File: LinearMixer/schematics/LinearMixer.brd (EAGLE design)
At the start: 49.7 x 98.7 mm, 65 parts, among them IC1 QUAD_OPAMPD, IC2 QUAD_OPAMPD, X1 53048-05, X2 53048-05, X5 53048-03, X6 53048-03, X7 53048-03

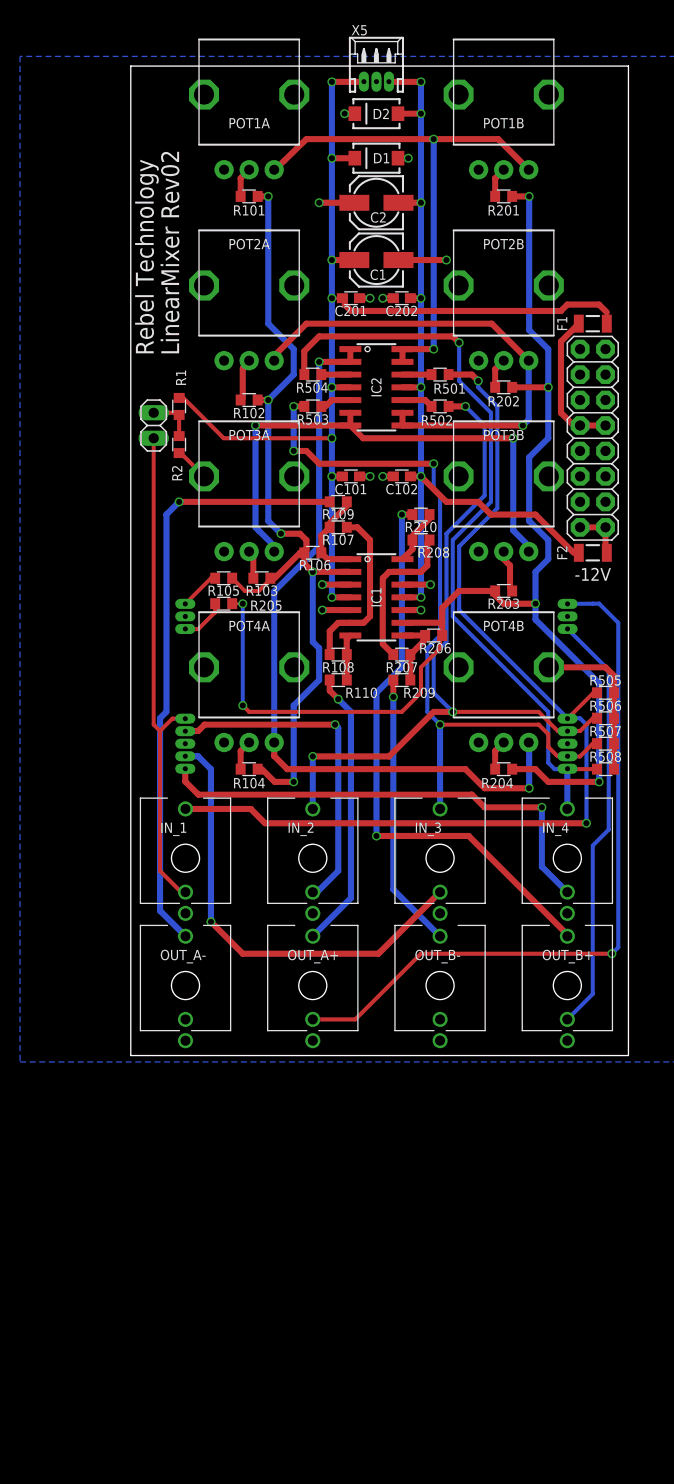
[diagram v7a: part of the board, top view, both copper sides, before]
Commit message: changed inverting outputs to hp
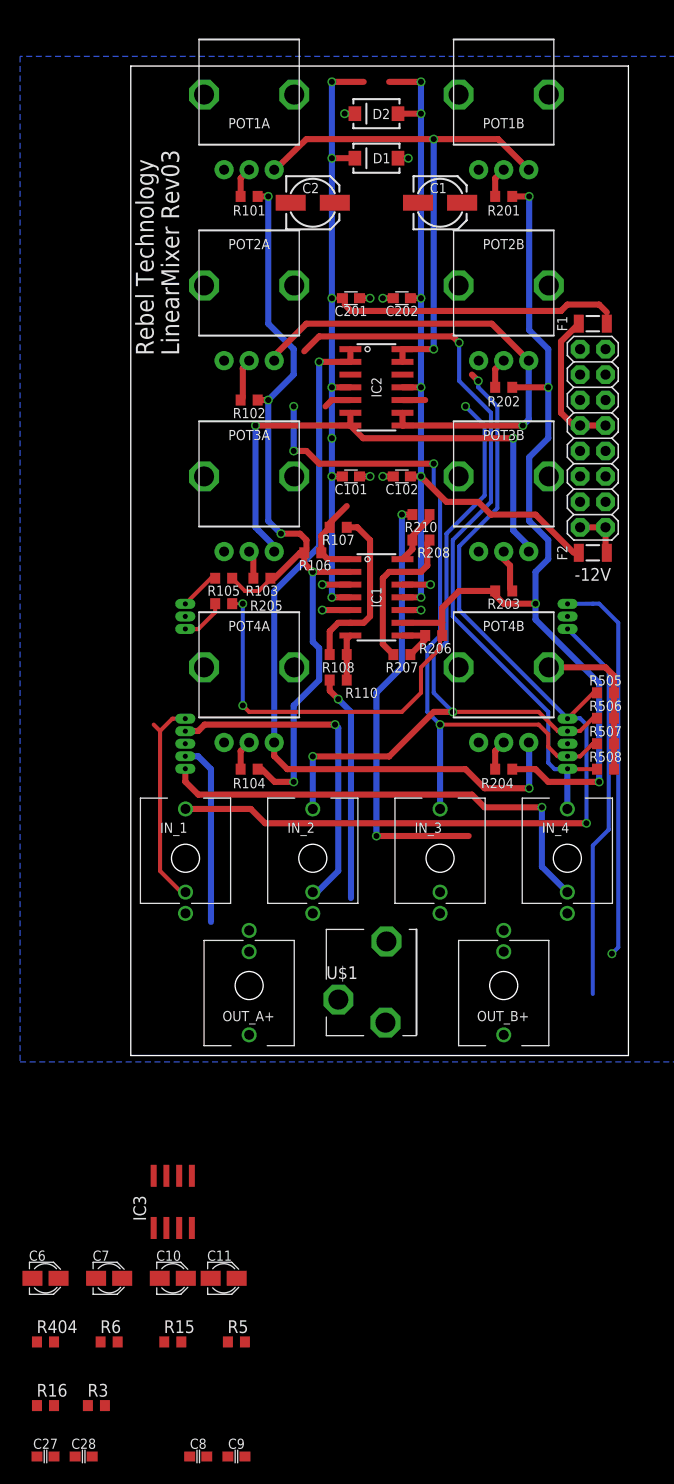
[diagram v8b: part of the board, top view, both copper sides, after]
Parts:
- removed JP1: (no value), pinhead:1X02
- removed OUT_A-, OUT_B-: THONKICONN, Rebel:THONKICONN
- removed R1, R2: 10k, resistor:R0603
- removed R109, R209: 100R, resistor:R0603
- removed R501, R502, R503, R504: 1k, resistor:R0603
- removed X5: 53048-03, con-molex:53048-03
- added C10, C11: 1uF, rcl:PANASONIC_A
- added C27, C28: 0.1uF, Rebel:C0603
- added C6, C7: 220uF, rcl:PANASONIC_A
- added C8, C9: 47nF, Rebel:C0603
- added IC3: NE5532D, linear:SO08
- added R15, R6: 100k, resistor:R0603
- added R16, R5: 4.7k, resistor:R0603
- added R3, R404: 10R, resistor:R0603
- added U$1: CON-PROSIGNAL_MJ-355W, Rebel:CON-PROSIGNAL_MJ-355W
- C1, C2: value 10u -> 22u
- R106, R206: value 200k -> 100k
- R107, R207: value 100k -> 51k
- moved C1 8.54 mm to (33.0, 85.7), turned to 0 degrees
- moved C2 6.35 mm to (20.3, 85.7), turned to 0 degrees
- moved OUT_B+ 6.35 mm to (39.4, 7.62), turned to 180 degrees
- moved OUT_A+ 6.35 mm to (14.0, 7.62), turned to 180 degrees
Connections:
- removed net N$1: IC1.1, R106.2, R107.1, R109.1
- removed net N$11: OUT_A-.P$3, R109.2
- removed net N$14: IC1.8, R206.2, R207.1, R209.1
- removed net N$17: OUT_B-.P$3, R209.2
- removed net N$42: IC2.3, R504.1
- removed net N$43: IC2.5, R503.1
- removed net N$48: IC2.10, R502.1
- removed net N$50: IC2.12, R501.1
- removed net N$7: JP1.1, R1.2, R2.1
- new net GND_A: U$1.P$1
- new net L_OUT: C6.-, U$1.P$2
- new net N$10: IC1.8, R15.2, R206.2, R207.1
- new net N$12: C9.2, R3.2
- new net N$13: IC1.1, R106.2, R107.1, R6.2
- new net N$2: C11.+, IC3.6
- new net N$21: C8.2, R404.2
- new net N$22: C6.+, C8.1, IC3.1
- new net N$28: C10.+, IC3.2
- new net N$3: C7.+, C9.1, IC3.7
- new net N$4: C11.-, R15.1, R16.2
- new net N$8: C10.-, R5.2, R6.1
- new net R_OUT: C7.-, U$1.P$3
- net +12V: now also C27.1, IC3.8; no longer R1.1, X5.3
- net -12V: now also C28.1, IC3.4; no longer X5.1
- net GND: now also C27.2, C28.2, IC3.3, IC3.5, R16.1, R3.1, R404.1, R5.1; no longer OUT_A-.P$1, OUT_B-.P$1, R2.2, X5.2
- net IN_1: now also IC2.12; no longer R501.2
- net IN_2: now also IC2.10; no longer R502.2
- net IN_3: now also IC2.5; no longer R503.2
- net IN_4: now also IC2.3; no longer R504.2
- net IN_SW_1: no longer JP1.2
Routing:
- net N$11: track 60.2 -> 0.00 mm, vias 1 -> 0
- net OUT_SW_A: track 71.7 -> 39.1 mm
- net IN_SW_1: track 49.9 -> 21.3 mm
- net N$17: track 27.5 -> 0.00 mm, vias 1 -> 0
- net IN_SW_3: track 45.1 -> 18.3 mm, vias 1 -> 0
- net +12V: track 110.8 -> 91.6 mm, vias 8 -> 7
- net N$15: track 57.5 -> 43.4 mm
- net GND: track 44.4 -> 32.7 mm, vias 12 -> 10
- net N$1: track 9.30 -> 0.00 mm
- net N$13: track 0.00 -> 8.88 mm
- net N$14: track 7.32 -> 0.00 mm
- net N$9: track 28.0 -> 22.6 mm
- net N$10: track 0.00 -> 4.78 mm
- net N$7: track 4.74 -> 0.00 mm
- net OUT_SW_B: track 42.4 -> 38.8 mm
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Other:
- board text added: "LinearMixer Rev03"
